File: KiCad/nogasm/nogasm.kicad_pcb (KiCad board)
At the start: 4 copper layers, 80 x 80 mm, 80 parts, among them J1 Barrel_Jack, J2 AudioJack4, J3 USB_B_Micro, Q1 AP55N03K, SW1 SW_Push, SW2 Rotary_Encoder_Switch, SW3 SW_DIP_x04, SW4 SW_DIP_x01, U1 MPXV5100DP, U2 LD29150DT50R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

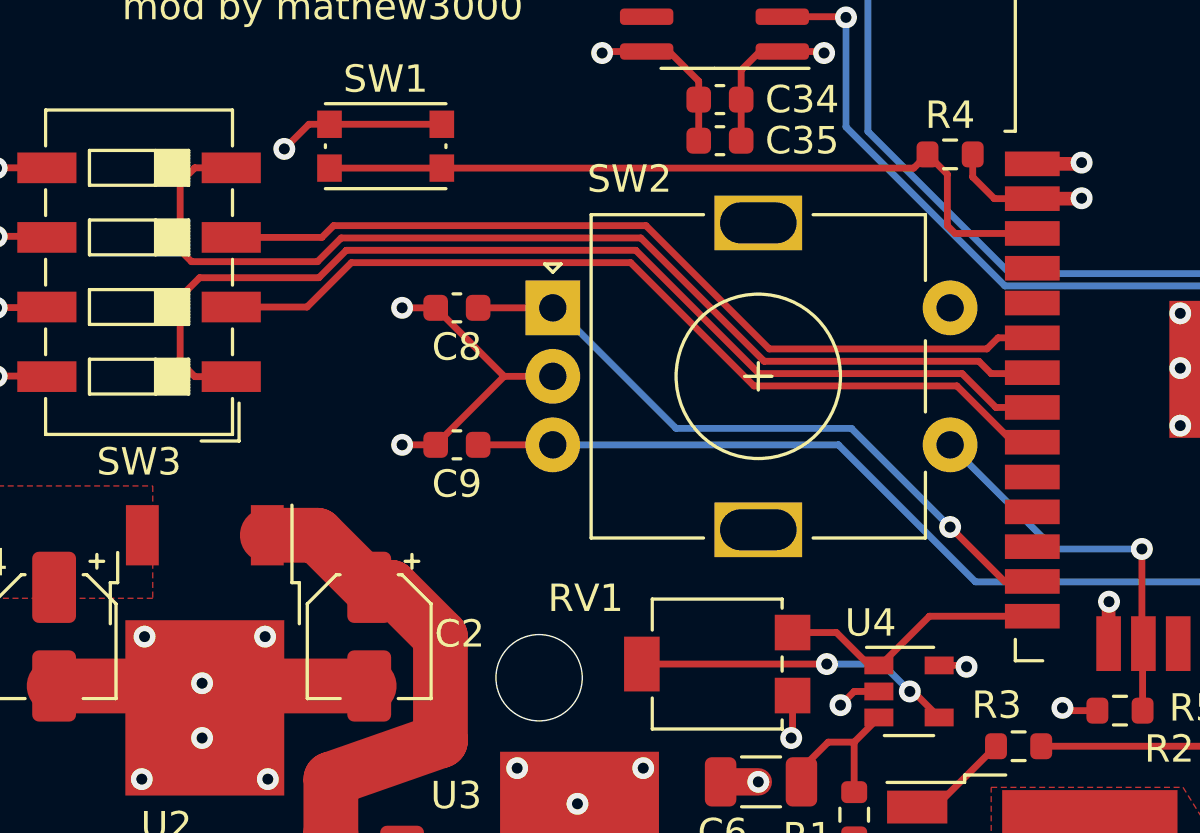
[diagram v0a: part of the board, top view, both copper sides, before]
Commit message: Updated PCB documents to fix ESP ADC channel
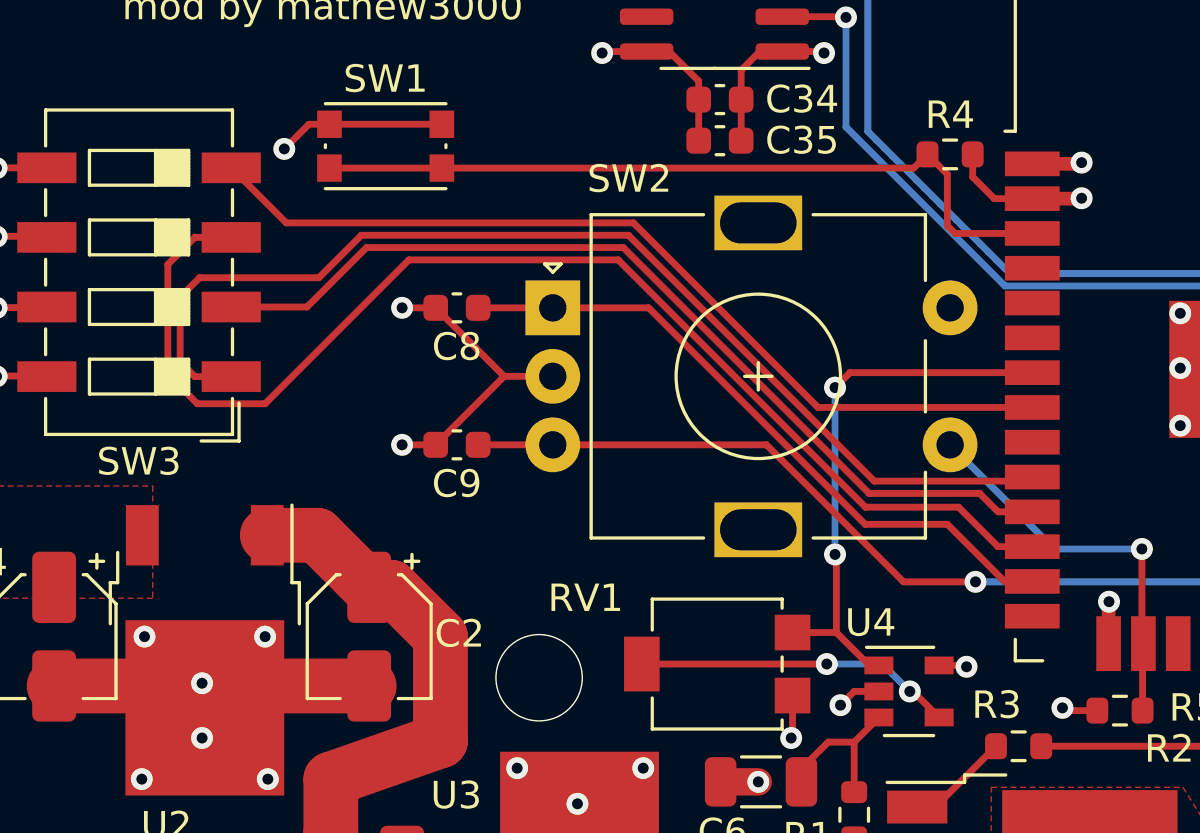
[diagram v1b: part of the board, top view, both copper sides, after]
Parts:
- U3: value BL1117-33CY -> LD29150DT33R
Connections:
- U5 pad 10: Net-(U5-Pad10) -> Net-(SW3-Pad1)
- U5 pad 11: Net-(U5-Pad11) -> Net-(SW3-Pad2)
- U5 pad 12: Net-(U5-Pad12) -> Net-(SW3-Pad3)
- U5 pad 14: /PRESSURE -> Net-(U5-Pad14)
- U5 pad 6: Net-(SW3-Pad3) -> Net-(U5-Pad6)
- U5 pad 7: Net-(SW3-Pad4) -> /PRESSURE
- U5 pad 8: Net-(SW3-Pad1) -> Net-(SW3-Pad4)
- U5 pad 9: Net-(SW3-Pad2) -> Net-(U5-Pad9)
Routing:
- net Net-(SW3-Pad3): track 31.4 -> 45.2 mm
- net /PRESSURE: track 10.1 -> 20.2 mm, vias 0 -> 2
- net Net-(SW3-Pad4): track 38.3 -> 32.9 mm
- net Net-(SW3-Pad1): track 38.6 -> 40.3 mm
- net Net-(SW3-Pad2): track 32.6 -> 34.1 mm
- net /ENC_A: track 24.4 -> 24.5 mm, vias 1 -> 0
- net /ENC_B: vias 1 -> 2
